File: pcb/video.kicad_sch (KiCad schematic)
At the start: 0 parts

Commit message: WIP
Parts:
- added X1: 25.175MHz, Oscillator:Oscillator_DIP-8_LargePads, symbol Oscillator:CXO_DIP8
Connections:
- new net Column Counter/CP: X1.5 (OUT)
- new net GND: X1.4 (GND)
- new net VCC: X1.8 (Vcc)
- no-connect marks 0 -> 1
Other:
- added sheet Column Counter (11bitcount.kicad_sch)
- added sheet Row Counter (11bitcount.kicad_sch)

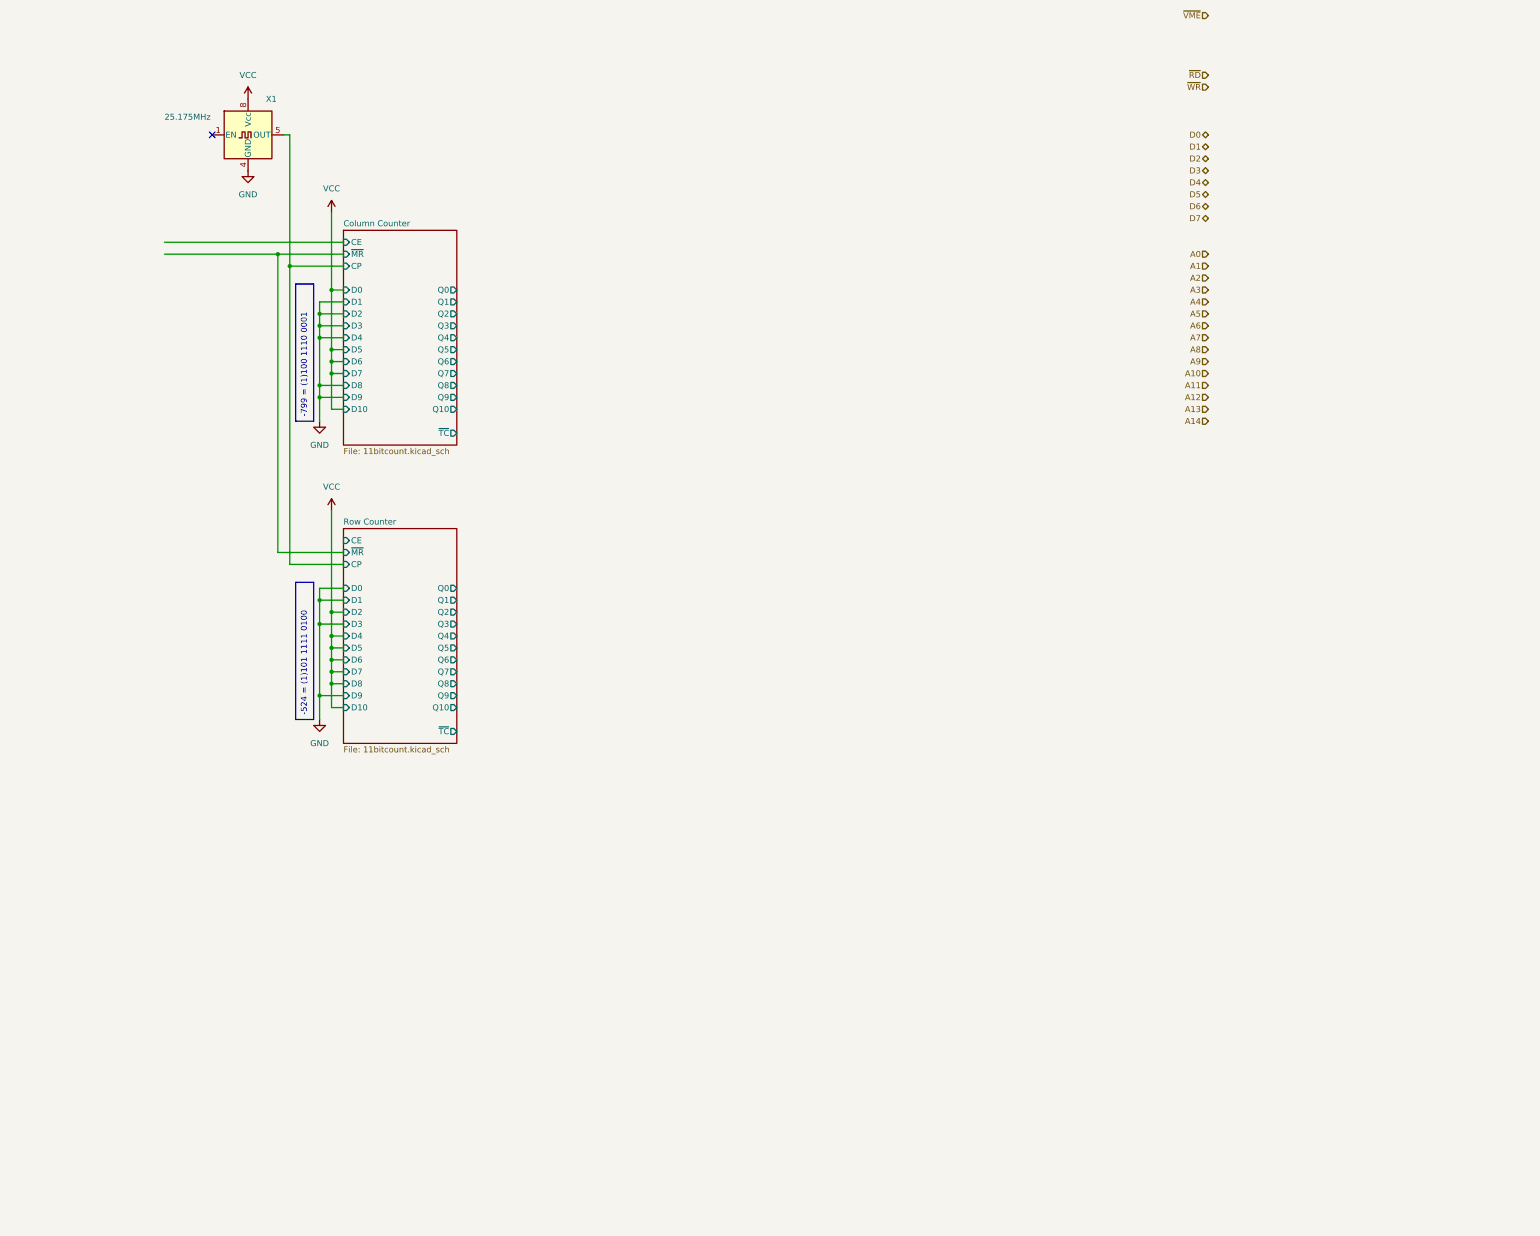
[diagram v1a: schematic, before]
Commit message: schematic: video signals, address counter, extra registers
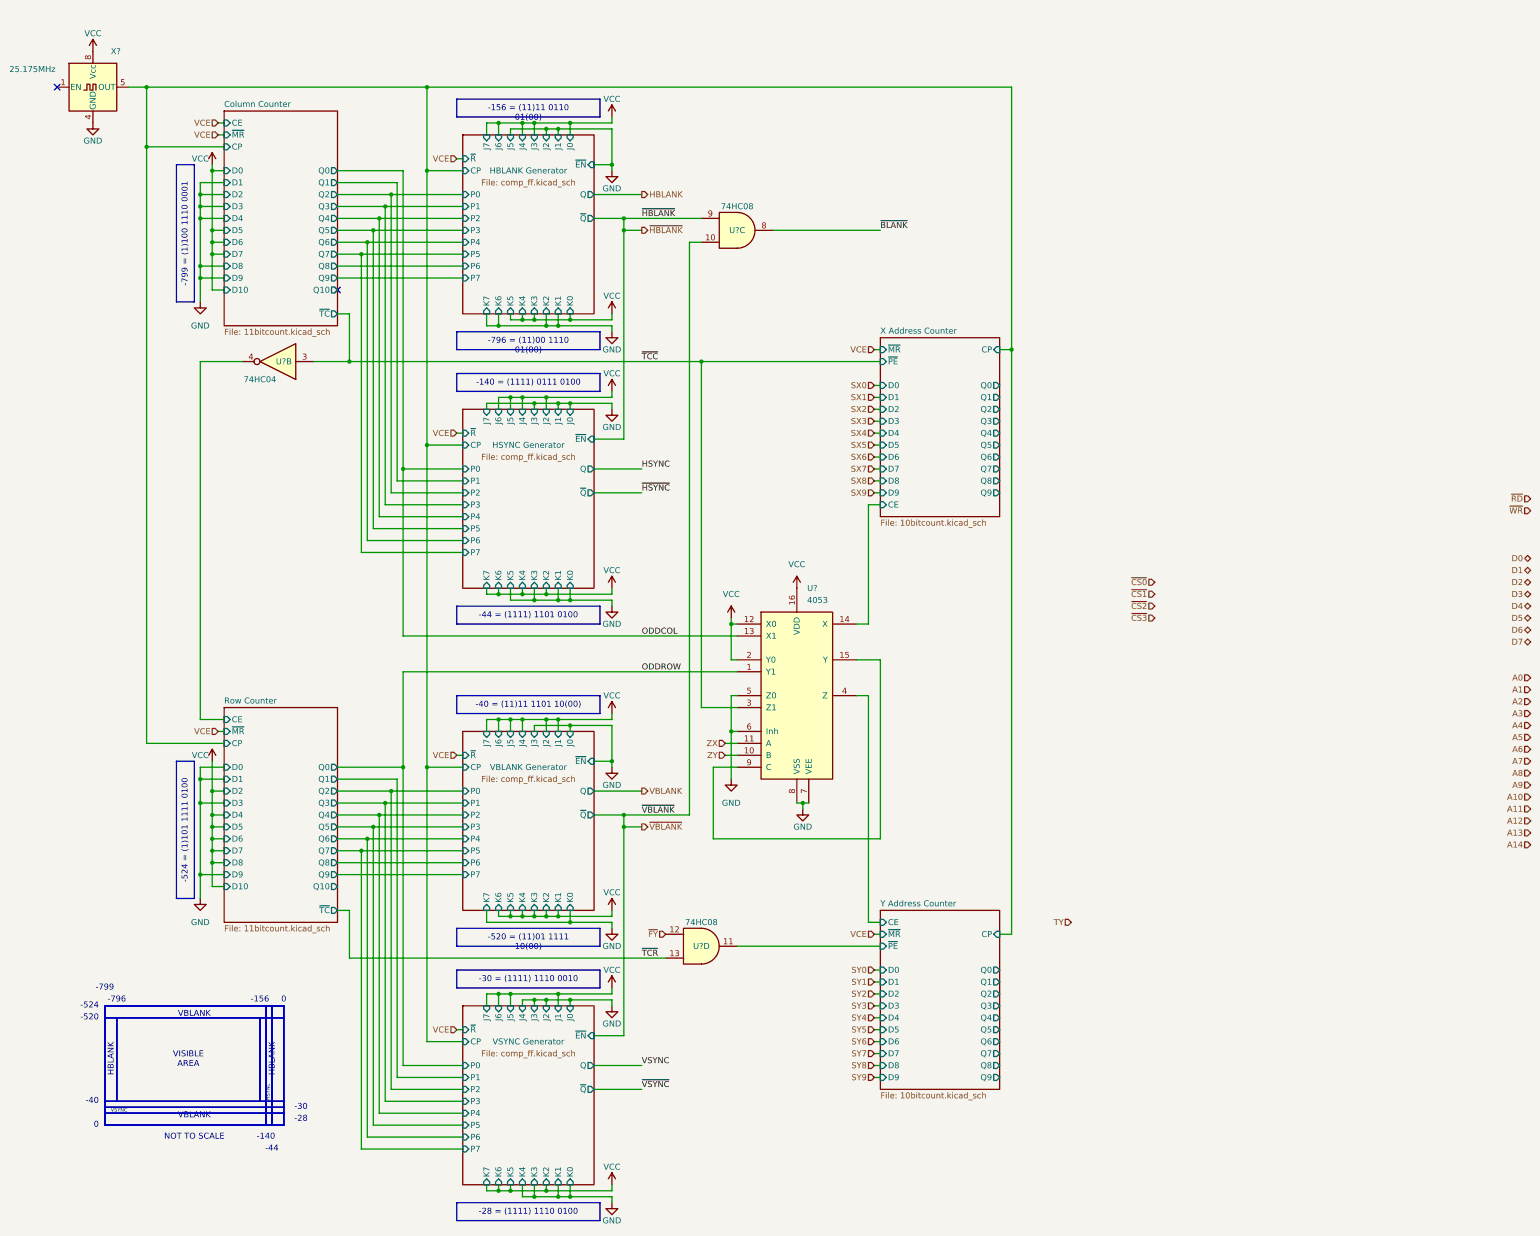
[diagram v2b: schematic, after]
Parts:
- added U? (x2): 74HC08, symbol 74xx:74LS08
- added U?: 4053, symbol 4xxx:4053
- added U?: 74HC04, symbol 74xx:74HC04
- renumbered X1 to X?
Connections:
- net GND: now also U?.5 (Z0), U?.6 (Inh), U?.7 (VEE), U?.8 (VSS)
- net Row Counter/CE: now also U?.4
- net VCC: now also U?.12 (X0), U?.16 (VDD), U?.2 (Y0)
- new net: U?.15 (Y), U?.9 (C)
- new net ODDCOL: U?.13 (X1)
- new net ODDROW: U?.1 (Y1)
- new net X Address Counter/CE: U?.14 (X)
- new net Y Address Counter/CE: U?.4 (Z)
- new net Y Address Counter/~{PE}: U?.11
- new net ZX: U?.11 (A)
- new net ZY: U?.10 (B)
- new net ~{BLANK}: U?.8
- new net ~{FY}: U?.12
- new net ~{HBLANK}: U?.9
- new net ~{TCC}: U?.3, U?.3 (Z1)
- new net ~{TCR}: U?.13
- new net ~{VBLANK}: U?.10
- no-connect marks 1 -> 2
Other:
- added sheet HBLANK Generator (comp_ff.kicad_sch)
- added sheet HSYNC Generator (comp_ff.kicad_sch)
- added sheet VBLANK Generator (comp_ff.kicad_sch)
- added sheet VSYNC Generator (comp_ff.kicad_sch)
- added sheet X Address Counter (10bitcount.kicad_sch)
- added sheet Y Address Counter (10bitcount.kicad_sch)
- note added: "-140"
- note added: "-156"
- note added: "-28"
- note added: "-30"
- note added: "-40"
- note added: "-44"
- note added: "-520"
- note added: "-524"
- note added: "-796"
- note added: "-799"
- note added: "0"
- note added: "HBLANK"
- note added: "HSYNC"
- note added: "NOT TO SCALE"
- note added: "VBLANK"
- note added: "VISIBLE AREA"
- note added: "VSYNC"
- moved on the sheet: X?

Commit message: WIP schematic
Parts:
- added U4: 74HC139, symbol 74xx:74LS139
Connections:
- new net Co-Processor/A13b: U4.13 (A1)
- new net Co-Processor/A14b: U4.14 (A0)
- new net Co-Processor/~{VME}b: U4.15 (E)
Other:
- added sheet Co-Processor (copro.kicad_sch)

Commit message: WIP schematic
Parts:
- gave numbers to parts that had none: 4
- renumbered U4 to U11
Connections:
- net VCC renamed +5V

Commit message: WIP PCB
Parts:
- renumbered U5 to U?, U10 to U?, U11 to U?, U9 to U?, X1 to X?

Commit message: wip schematic
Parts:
- removed U? (x2): 74HC08, symbol 74xx:74LS08
- removed U?: 74HC04, symbol 74xx:74HC04
- added J?: VGA, symbol Connector:DE15_Receptacle_HighDensity_MountingHoles
- added Q? (x3): 2N7000, Package_TO_SOT_THT:TO-92_Inline, symbol Transistor_FET:2N7000
- added R? (x3): 10 Ω, symbol Device:R_Small
- added U? (x4): 74HC00, symbol 74xx:74HC00
- added U? (x2): 74HC157, symbol 74xx:74LS157
- added U?: 74AC573, symbol 74xx:74LS573
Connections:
- net +5V: now also U?.16 (VCC), U?.16 (VCC), U?.20 (VCC)
- net Co-Processor/A13b: now also U?.14 (A0); no longer U?.13 (A1)
- net Co-Processor/A14b: now also U?.13 (A1); no longer U?.14 (A0)
- net Column Counter/CP: now also U?.11 (Load)
- net GND: now also J?.0, J?.10, J?.5, J?.6, J?.7, J?.8, Q?.1 (S), Q?.1 (S), Q?.1 (S), U?.10 (GND), U?.10 (I1c), U?.11 (I0c), U?.13 (I1d), U?.14 (I0d), U?.15 (E), U?.15 (E), U?.8 (GND), U?.8 (GND)
- net Row Counter/CE: now also U?.6
- net TY: now also U?.1 (S)
- net Y Address Counter/Q0: now also U?.1 (S)
- net Y Address Counter/Q3: now also U?.2 (I0a), U?.6 (I1b)
- net Y Address Counter/Q9: now also U?.3 (I1a), U?.5 (I0b)
- net Y Address Counter/~{PE}: now also U?.8
- net ~{FY}: now also U?.12
- net ~{HBLANK}: now also U?.1
- net ~{HSYNC}: now also J?.13
- net ~{TCC}: now also U?.4, U?.5
- net ~{TCR}: now also U?.13
- net ~{VBLANK}: now also U?.2
- net ~{VSYNC}: now also J?.14
- net Pattern Table/~{CE}: now reaches U?.10 (O2)
- net Attribute Table/~{CE}: now reaches U?.11 (O1)
- net Name Table/~{CE}: now reaches U?.12 (O0)
- net Color Table/~{CE}: now reaches U?.9 (O3)
- new net: Q?.2 (G), R?.2 (x3)
- new net: U?.10, U?.11, U?.9
- new net Attribute Table/A7: U?.4 (Za)
- new net B0: U?.17 (Q2)
- new net B1: U?.16 (Q3)
- new net BLANK: R?.1, R?.1, R?.1, U?.1 (OE), U?.3
- new net Color Table/A0: U?.4 (Za)
- new net Color Table/A1: U?.7 (Zb)
- new net Color Table/A12: U?.7 (Zb)
- new net Color Table/A2: U?.9 (Zc)
- new net Color Table/A3: U?.12 (Zd)
- new net Color Table/Q0: U?.2 (D0)
- new net Color Table/Q1: U?.3 (D1)
- new net Color Table/Q2: U?.4 (D2)
- new net Color Table/Q3: U?.5 (D3)
- new net Color Table/Q4: U?.6 (D4)
- new net Color Table/Q5: U?.7 (D5)
- new net Color Table/Q6: U?.8 (D6)
- new net Color Table/Q7: U?.9 (D7)
- new net G0: U?.15 (Q4)
- new net G1: U?.14 (Q5)
- new net I0: U?.19 (Q0)
- new net I1: U?.18 (Q1)
- new net Pattern Table/Q0: U?.2 (I0a)
- new net Pattern Table/Q1: U?.5 (I0b)
- new net Pattern Table/Q2: U?.11 (I0c)
- new net Pattern Table/Q3: U?.14 (I0d)
- new net Pattern Table/Q4: U?.3 (I1a)
- new net Pattern Table/Q5: U?.6 (I1b)
- new net Pattern Table/Q6: U?.10 (I1c)
- new net Pattern Table/Q7: U?.13 (I1d)
- new net R0: U?.13 (Q6)
- new net R1: U?.12 (Q7)
- new net R2R Blue/OUT: J?.3, Q?.3 (D)
- new net R2R Green/OUT: J?.2, Q?.3 (D)
- new net R2R Red/OUT: J?.1, Q?.3 (D)
- no-connect marks 2 -> 9
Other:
- added sheet Attribute Table (vram8k.kicad_sch)
- added sheet Color Table (vram8k.kicad_sch)
- added sheet Name Table (vram8k.kicad_sch)
- added sheet Pattern Table (vram8k.kicad_sch)
- added sheet R2R Blue (r2r.kicad_sch)
- added sheet R2R Green (r2r.kicad_sch)
- added sheet R2R Red (r2r.kicad_sch)
- moved on the sheet: U?, U?B, X?

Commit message: PCB: add reset circuit, xtal
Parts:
- added R6: 220kΩ, symbol Device:R
- R7, R8, R9: renamed from R?; value 10 Ω -> 10Ω
- gave numbers to parts that had none: 11
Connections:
- net +5V: now also R6.1
- net Co-Processor/~{VME}b: now also R6.2
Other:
- sheet Co-Processor ports: added ~{VMAP}; removed VMAP
- moved on the sheet: U12B

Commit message: WIP schematic
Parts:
- renumbered Q1 to Q4, Q2 to Q5, Q3 to Q6, R6 to R13, R7 to R14, R8 to R15, R9 to R16, U9 to U10, U10 to U11, U11 to U12, U12 to U13, U13 to U14, U14 to U15
